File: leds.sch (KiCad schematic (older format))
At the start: 32 parts

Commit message: start working on spokes
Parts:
- added D33, D34, D35, D36, D37, D38, D39, D40, D41, D42, D43, D44, D45, D46, D47, D48, D49, D50, D51, D52, D53, D54, D55, D56, D57, D58, D59, D60, D61, D62, D63, D64, D65, D66, D67, D68, D69, D70, D71, D72, D73, D74, D75, D76, D77, D78, D79, D80, D? (x16): APA102-2020, LED_SMD:LED-APA102-2020_tightened_pads, symbol LED:APA102-2020
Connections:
- net +5V: now also D33.1 (VDD), D34.1 (VDD), D35.1 (VDD), D36.1 (VDD), D37.1 (VDD), D38.1 (VDD), D39.1 (VDD), D40.1 (VDD), D41.1 (VDD), D42.1 (VDD), D43.1 (VDD), D44.1 (VDD), D45.1 (VDD), D46.1 (VDD), D47.1 (VDD), D48.1 (VDD), D49.1 (VDD), D50.1 (VDD), D51.1 (VDD), D52.1 (VDD), D53.1 (VDD), D54.1 (VDD), D55.1 (VDD), D56.1 (VDD), D57.1 (VDD), D58.1 (VDD), D59.1 (VDD), D60.1 (VDD), D61.1 (VDD), D62.1 (VDD), D63.1 (VDD), D64.1 (VDD), D65.1 (VDD), D66.1 (VDD), D67.1 (VDD), D68.1 (VDD), D69.1 (VDD), D70.1 (VDD), D71.1 (VDD), D72.1 (VDD), D73.1 (VDD), D74.1 (VDD), D75.1 (VDD), D76.1 (VDD), D77.1 (VDD), D78.1 (VDD), D79.1 (VDD), D80.1 (VDD), D?.1 (VDD), D?.1 (VDD), D?.1 (VDD), D?.1 (VDD), D?.1 (VDD), D?.1 (VDD), D?.1 (VDD), D?.1 (VDD), D?.1 (VDD), D?.1 (VDD), D?.1 (VDD), D?.1 (VDD), D?.1 (VDD), D?.1 (VDD), D?.1 (VDD), D?.1 (VDD)
- net GND: now also D33.6 (GND), D34.6 (GND), D35.6 (GND), D36.6 (GND), D37.6 (GND), D38.6 (GND), D39.6 (GND), D40.6 (GND), D41.6 (GND), D42.6 (GND), D43.6 (GND), D44.6 (GND), D45.6 (GND), D46.6 (GND), D47.6 (GND), D48.6 (GND), D49.6 (GND), D50.6 (GND), D51.6 (GND), D52.6 (GND), D53.6 (GND), D54.6 (GND), D55.6 (GND), D56.6 (GND), D57.6 (GND), D58.6 (GND), D59.6 (GND), D60.6 (GND), D61.6 (GND), D62.6 (GND), D63.6 (GND), D64.6 (GND), D65.6 (GND), D66.6 (GND), D67.6 (GND), D68.6 (GND), D69.6 (GND), D70.6 (GND), D71.6 (GND), D72.6 (GND), D73.6 (GND), D74.6 (GND), D75.6 (GND), D76.6 (GND), D77.6 (GND), D78.6 (GND), D79.6 (GND), D80.6 (GND), D?.6 (GND), D?.6 (GND), D?.6 (GND), D?.6 (GND), D?.6 (GND), D?.6 (GND), D?.6 (GND), D?.6 (GND), D?.6 (GND), D?.6 (GND), D?.6 (GND), D?.6 (GND), D?.6 (GND), D?.6 (GND), D?.6 (GND), D?.6 (GND)
- net D32_CKO: now reaches D32.2 (CKO)
- net D32_CKO: now also D33.5 (CKI)
- net D32_SDO: now reaches D32.3 (SDO)
- net D32_SDO: now also D33.4 (SDI)
- net SCK renamed LED_SCK
- net SDO renamed LED_DATA
- new net: D48.2 (CKO), D49.5 (CKI)
- new net: D48.3 (SDO), D49.4 (SDI)
- new net: D47.3 (SDO), D48.4 (SDI)
- new net: D47.2 (CKO), D48.5 (CKI)
- new net: D46.3 (SDO), D47.4 (SDI)
- new net: D46.2 (CKO), D47.5 (CKI)
- new net: D45.3 (SDO), D46.4 (SDI)
- new net: D45.2 (CKO), D46.5 (CKI)
- new net: D44.3 (SDO), D45.4 (SDI)
- new net: D44.2 (CKO), D45.5 (CKI)
- new net: D43.3 (SDO), D44.4 (SDI)
- new net: D43.2 (CKO), D44.5 (CKI)
- new net: D42.3 (SDO), D43.4 (SDI)
- new net: D42.2 (CKO), D43.5 (CKI)
- new net: D41.3 (SDO), D42.4 (SDI)
- new net: D41.2 (CKO), D42.5 (CKI)
- new net: D40.3 (SDO), D41.4 (SDI)
- new net: D40.2 (CKO), D41.5 (CKI)
- new net: D39.3 (SDO), D40.4 (SDI)
- new net: D39.2 (CKO), D40.5 (CKI)
- new net: D38.3 (SDO), D39.4 (SDI)
- new net: D38.2 (CKO), D39.5 (CKI)
- new net: D37.3 (SDO), D38.4 (SDI)
- new net: D37.2 (CKO), D38.5 (CKI)
- new net: D36.3 (SDO), D37.4 (SDI)
- new net: D36.2 (CKO), D37.5 (CKI)
- new net: D35.3 (SDO), D36.4 (SDI)
- new net: D35.2 (CKO), D36.5 (CKI)
- new net: D34.3 (SDO), D35.4 (SDI)
- new net: D34.2 (CKO), D35.5 (CKI)
- new net: D33.3 (SDO), D34.4 (SDI)
- new net: D33.2 (CKO), D34.5 (CKI)
- new net: D49.2 (CKO), D50.5 (CKI)
- new net: D49.3 (SDO), D50.4 (SDI)
- new net: D50.2 (CKO), D51.5 (CKI)
- new net: D50.3 (SDO), D51.4 (SDI)
- new net: D51.2 (CKO), D52.5 (CKI)
- new net: D51.3 (SDO), D52.4 (SDI)
- new net: D52.2 (CKO), D53.5 (CKI)
- new net: D52.3 (SDO), D53.4 (SDI)
- new net: D53.2 (CKO), D54.5 (CKI)
- new net: D53.3 (SDO), D54.4 (SDI)
- new net: D54.2 (CKO), D55.5 (CKI)
- new net: D54.3 (SDO), D55.4 (SDI)
- new net: D55.2 (CKO), D56.5 (CKI)
- new net: D55.3 (SDO), D56.4 (SDI)
- new net: D56.2 (CKO), D57.5 (CKI)
- new net: D56.3 (SDO), D57.4 (SDI)
- new net: D57.2 (CKO), D58.5 (CKI)
- new net: D57.3 (SDO), D58.4 (SDI)
- new net: D58.2 (CKO), D59.5 (CKI)
- new net: D58.3 (SDO), D59.4 (SDI)
- new net: D59.2 (CKO), D60.5 (CKI)
- new net: D59.3 (SDO), D60.4 (SDI)
- new net: D60.2 (CKO), D61.5 (CKI)
- new net: D60.3 (SDO), D61.4 (SDI)
- new net: D61.2 (CKO), D62.5 (CKI)
- new net: D61.3 (SDO), D62.4 (SDI)
- new net: D62.2 (CKO), D63.5 (CKI)
- new net: D62.3 (SDO), D63.4 (SDI)
- new net: D63.2 (CKO), D64.5 (CKI)
- new net: D63.3 (SDO), D64.4 (SDI)
- new net: D80.2 (CKO), D?.5 (CKI)
- new net: D80.3 (SDO), D?.4 (SDI)
- new net: D79.3 (SDO), D80.4 (SDI)
- new net: D79.2 (CKO), D80.5 (CKI)
- new net: D78.3 (SDO), D79.4 (SDI)
- new net: D78.2 (CKO), D79.5 (CKI)
- new net: D77.3 (SDO), D78.4 (SDI)
- new net: D77.2 (CKO), D78.5 (CKI)
- new net: D76.3 (SDO), D77.4 (SDI)
- new net: D76.2 (CKO), D77.5 (CKI)
- new net: D75.3 (SDO), D76.4 (SDI)
- new net: D75.2 (CKO), D76.5 (CKI)
- new net: D74.3 (SDO), D75.4 (SDI)
- new net: D74.2 (CKO), D75.5 (CKI)
- new net: D73.3 (SDO), D74.4 (SDI)
- new net: D73.2 (CKO), D74.5 (CKI)
- new net: D72.3 (SDO), D73.4 (SDI)
- new net: D72.2 (CKO), D73.5 (CKI)
- new net: D71.3 (SDO), D72.4 (SDI)
- new net: D71.2 (CKO), D72.5 (CKI)
- new net: D70.3 (SDO), D71.4 (SDI)
- new net: D70.2 (CKO), D71.5 (CKI)
- new net: D69.3 (SDO), D70.4 (SDI)
- new net: D69.2 (CKO), D70.5 (CKI)
- new net: D68.3 (SDO), D69.4 (SDI)
- new net: D68.2 (CKO), D69.5 (CKI)
- new net: D67.3 (SDO), D68.4 (SDI)
- new net: D67.2 (CKO), D68.5 (CKI)
- new net: D66.3 (SDO), D67.4 (SDI)
- new net: D66.2 (CKO), D67.5 (CKI)
- new net: D65.3 (SDO), D66.4 (SDI)
- new net: D65.2 (CKO), D66.5 (CKI)
- new net: D?.2 (CKO), D?.5 (CKI) (x15)
- new net: D?.3 (SDO), D?.4 (SDI) (x15)
- new net D64_CKO: D64.2 (CKO), D65.5 (CKI)
- new net D64_SDO: D64.3 (SDO), D65.4 (SDI)

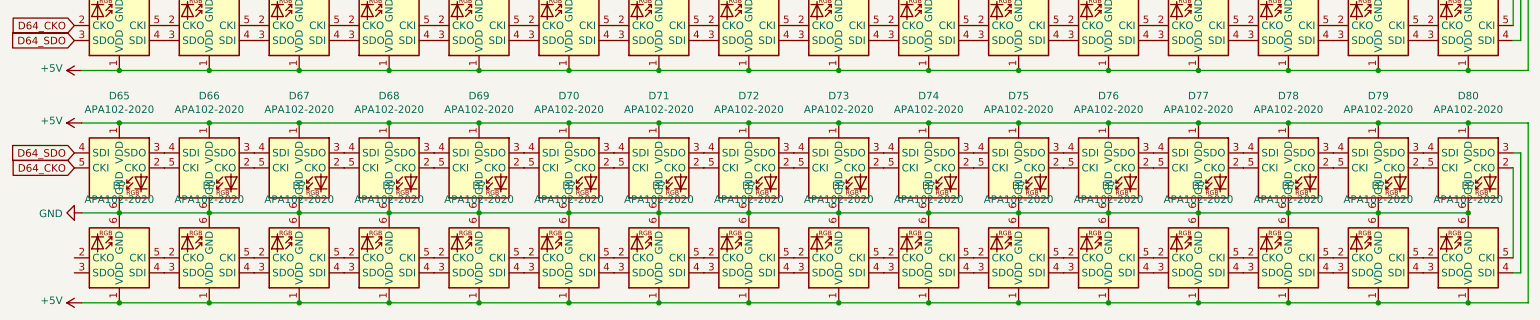
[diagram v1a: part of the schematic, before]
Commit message: clean up various point-like object types; tweak Edge.Cuts to be precise overlap in order to fix pcbnew thinking it wasn't a closed shape, but turns out this was also a bug fixed in kicad-5.1.3 so I'm not sure if this change was actually necessary, but it works now
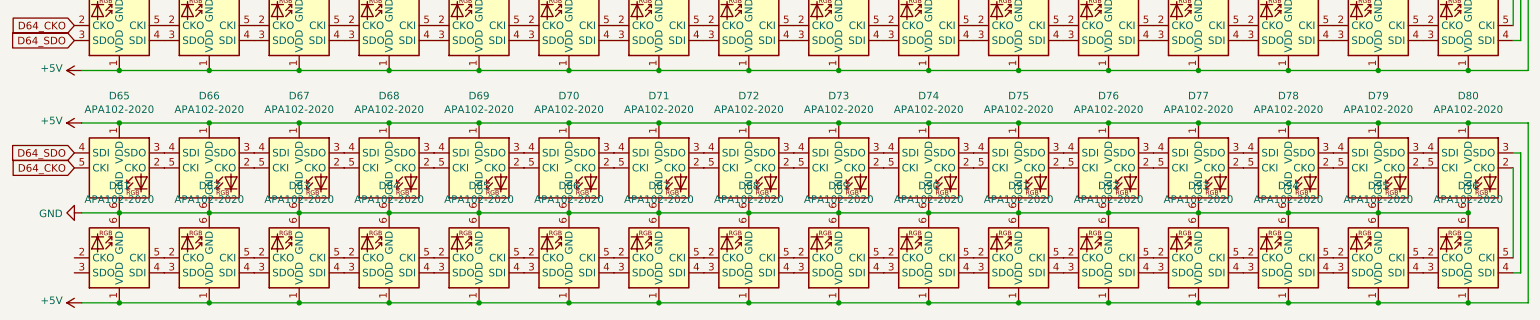
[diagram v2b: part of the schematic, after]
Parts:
- gave numbers to parts that had none: 16
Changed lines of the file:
@@
 P 10100 4900
 AR Path="/5F992E17" Ref="D?"  Part="1"
-AR Path="/5F81AC32/5F992E17" Ref="D?"  Part="1"
-F 0 "D?" H 10100 4419 50  0000 C CNN
+AR Path="/5F81AC32/5F992E17" Ref="D96"  Part="1"
+F 0 "D96" H 10100 4419 50  0000 C CNN
 F 1 "APA102-2020" H 10100 4510 50  0000 C CNN
 F 2 "LED_SMD:LED-APA102-2020_tightened_pads" H 10150 4600 50  0001 L TNN
@@
 P 9500 4900
 AR Path="/5F992E1D" Ref="D?"  Part="1"
-AR Path="/5F81AC32/5F992E1D" Ref="D?"  Part="1"
-F 0 "D?" H 9500 4419 50  0000 C CNN
+AR Path="/5F81AC32/5F992E1D" Ref="D95"  Part="1"
+F 0 "D95" H 9500 4419 50  0000 C CNN
 F 1 "APA102-2020" H 9500 4510 50  0000 C CNN
 F 2 "LED_SMD:LED-APA102-2020_tightened_pads" H 9550 4600 50  0001 L TNN
@@
 P 8900 4900
 AR Path="/5F992E26" Ref="D?"  Part="1"
-AR Path="/5F81AC32/5F992E26" Ref="D?"  Part="1"
-F 0 "D?" H 8900 4419 50  0000 C CNN
+AR Path="/5F81AC32/5F992E26" Ref="D94"  Part="1"
+F 0 "D94" H 8900 4419 50  0000 C CNN
 F 1 "APA102-2020" H 8900 4510 50  0000 C CNN
 F 2 "LED_SMD:LED-APA102-2020_tightened_pads" H 8950 4600 50  0001 L TNN
@@
 P 8300 4900
 AR Path="/5F992E2C" Ref="D?"  Part="1"
-AR Path="/5F81AC32/5F992E2C" Ref="D?"  Part="1"
-F 0 "D?" H 8300 4419 50  0000 C CNN
+AR Path="/5F81AC32/5F992E2C" Ref="D93"  Part="1"
+F 0 "D93" H 8300 4419 50  0000 C CNN
 F 1 "APA102-2020" H 8300 4510 50  0000 C CNN
 F 2 "LED_SMD:LED-APA102-2020_tightened_pads" H 8350 4600 50  0001 L TNN
@@
 P 7700 4900
 AR Path="/5F992E32" Ref="D?"  Part="1"
-AR Path="/5F81AC32/5F992E32" Ref="D?"  Part="1"
-F 0 "D?" H 7700 4419 50  0000 C CNN
+AR Path="/5F81AC32/5F992E32" Ref="D92"  Part="1"
+F 0 "D92" H 7700 4419 50  0000 C CNN
 F 1 "APA102-2020" H 7700 4510 50  0000 C CNN
 F 2 "LED_SMD:LED-APA102-2020_tightened_pads" H 7750 4600 50  0001 L TNN
@@
 P 7100 4900
 AR Path="/5F992E38" Ref="D?"  Part="1"
-AR Path="/5F81AC32/5F992E38" Ref="D?"  Part="1"
-F 0 "D?" H 7100 4419 50  0000 C CNN
+AR Path="/5F81AC32/5F992E38" Ref="D91"  Part="1"
+F 0 "D91" H 7100 4419 50  0000 C CNN
 F 1 "APA102-2020" H 7100 4510 50  0000 C CNN
 F 2 "LED_SMD:LED-APA102-2020_tightened_pads" H 7150 4600 50  0001 L TNN
@@
 P 6500 4900
 AR Path="/5F992E3E" Ref="D?"  Part="1"
-AR Path="/5F81AC32/5F992E3E" Ref="D?"  Part="1"
-F 0 "D?" H 6500 4419 50  0000 C CNN
+AR Path="/5F81AC32/5F992E3E" Ref="D90"  Part="1"
+F 0 "D90" H 6500 4419 50  0000 C CNN
 F 1 "APA102-2020" H 6500 4510 50  0000 C CNN
 F 2 "LED_SMD:LED-APA102-2020_tightened_pads" H 6550 4600 50  0001 L TNN
@@
 P 5900 4900
 AR Path="/5F992E44" Ref="D?"  Part="1"
-AR Path="/5F81AC32/5F992E44" Ref="D?"  Part="1"
-F 0 "D?" H 5900 4419 50  0000 C CNN
+AR Path="/5F81AC32/5F992E44" Ref="D89"  Part="1"
+F 0 "D89" H 5900 4419 50  0000 C CNN
 F 1 "APA102-2020" H 5900 4510 50  0000 C CNN
 F 2 "LED_SMD:LED-APA102-2020_tightened_pads" H 5950 4600 50  0001 L TNN
@@
 P 5300 4900
 AR Path="/5F992E4A" Ref="D?"  Part="1"
-AR Path="/5F81AC32/5F992E4A" Ref="D?"  Part="1"
-F 0 "D?" H 5300 4419 50  0000 C CNN
+AR Path="/5F81AC32/5F992E4A" Ref="D88"  Part="1"
+F 0 "D88" H 5300 4419 50  0000 C CNN
 F 1 "APA102-2020" H 5300 4510 50  0000 C CNN
 F 2 "LED_SMD:LED-APA102-2020_tightened_pads" H 5350 4600 50  0001 L TNN
@@
 P 4700 4900
 AR Path="/5F992E50" Ref="D?"  Part="1"
-AR Path="/5F81AC32/5F992E50" Ref="D?"  Part="1"
-F 0 "D?" H 4700 4419 50  0000 C CNN
+AR Path="/5F81AC32/5F992E50" Ref="D87"  Part="1"
+F 0 "D87" H 4700 4419 50  0000 C CNN
 F 1 "APA102-2020" H 4700 4510 50  0000 C CNN
 F 2 "LED_SMD:LED-APA102-2020_tightened_pads" H 4750 4600 50  0001 L TNN
@@
 P 4100 4900
 AR Path="/5F992E56" Ref="D?"  Part="1"
-AR Path="/5F81AC32/5F992E56" Ref="D?"  Part="1"
-F 0 "D?" H 4100 4419 50  0000 C CNN
+AR Path="/5F81AC32/5F992E56" Ref="D86"  Part="1"
+F 0 "D86" H 4100 4419 50  0000 C CNN
 F 1 "APA102-2020" H 4100 4510 50  0000 C CNN
 F 2 "LED_SMD:LED-APA102-2020_tightened_pads" H 4150 4600 50  0001 L TNN
@@
 P 3500 4900
 AR Path="/5F992E5C" Ref="D?"  Part="1"
-AR Path="/5F81AC32/5F992E5C" Ref="D?"  Part="1"
-F 0 "D?" H 3500 4419 50  0000 C CNN
+AR Path="/5F81AC32/5F992E5C" Ref="D85"  Part="1"
+F 0 "D85" H 3500 4419 50  0000 C CNN
 F 1 "APA102-2020" H 3500 4510 50  0000 C CNN
 F 2 "LED_SMD:LED-APA102-2020_tightened_pads" H 3550 4600 50  0001 L TNN
@@
 P 2900 4900
 AR Path="/5F992E62" Ref="D?"  Part="1"
-AR Path="/5F81AC32/5F992E62" Ref="D?"  Part="1"
-F 0 "D?" H 2900 4419 50  0000 C CNN
+AR Path="/5F81AC32/5F992E62" Ref="D84"  Part="1"
+F 0 "D84" H 2900 4419 50  0000 C CNN
 F 1 "APA102-2020" H 2900 4510 50  0000 C CNN
 F 2 "LED_SMD:LED-APA102-2020_tightened_pads" H 2950 4600 50  0001 L TNN
@@
 P 2300 4900
 AR Path="/5F992E68" Ref="D?"  Part="1"
-AR Path="/5F81AC32/5F992E68" Ref="D?"  Part="1"
-F 0 "D?" H 2300 4419 50  0000 C CNN
+AR Path="/5F81AC32/5F992E68" Ref="D83"  Part="1"
+F 0 "D83" H 2300 4419 50  0000 C CNN
 F 1 "APA102-2020" H 2300 4510 50  0000 C CNN
 F 2 "LED_SMD:LED-APA102-2020_tightened_pads" H 2350 4600 50  0001 L TNN
@@
 P 1700 4900
 AR Path="/5F992E6E" Ref="D?"  Part="1"
-AR Path="/5F81AC32/5F992E6E" Ref="D?"  Part="1"
-F 0 "D?" H 1700 4419 50  0000 C CNN
+AR Path="/5F81AC32/5F992E6E" Ref="D82"  Part="1"
+F 0 "D82" H 1700 4419 50  0000 C CNN
 F 1 "APA102-2020" H 1700 4510 50  0000 C CNN
 F 2 "LED_SMD:LED-APA102-2020_tightened_pads" H 1750 4600 50  0001 L TNN
@@
 P 1100 4900
 AR Path="/5F992E74" Ref="D?"  Part="1"
-AR Path="/5F81AC32/5F992E74" Ref="D?"  Part="1"
-F 0 "D?" H 1100 4419 50  0000 C CNN
+AR Path="/5F81AC32/5F992E74" Ref="D81"  Part="1"
+F 0 "D81" H 1100 4419 50  0000 C CNN
 F 1 "APA102-2020" H 1100 4510 50  0000 C CNN
 F 2 "LED_SMD:LED-APA102-2020_tightened_pads" H 1150 4600 50  0001 L TNN
@@
 $EndComp
 $Comp
-L power:+5V #PWR?
+L power:+5V #PWR0124
 U 1 1 5F992E7A
 P 850 5200
-F 0 "#PWR?" H 850 5050 50  0001 C CNN
+F 0 "#PWR0124" H 850 5050 50  0001 C CNN
 F 1 "+5V" V 865 5328 50  0000 L CNN
 F 2 "" H 850 5200 50  0001 C CNN
@@
 	1100 4600 850  4600
 $Comp
-L power:GND #PWR?
+L power:GND #PWR0125
 U 1 1 5F9ECE1D
 P 850 3050
-F 0 "#PWR?" H 850 2800 50  0001 C CNN
+F 0 "#PWR0125" H 850 2800 50  0001 C CNN
 F 1 "GND" V 855 2922 50  0000 R CNN
 F 2 "" H 850 3050 50  0001 C CNN

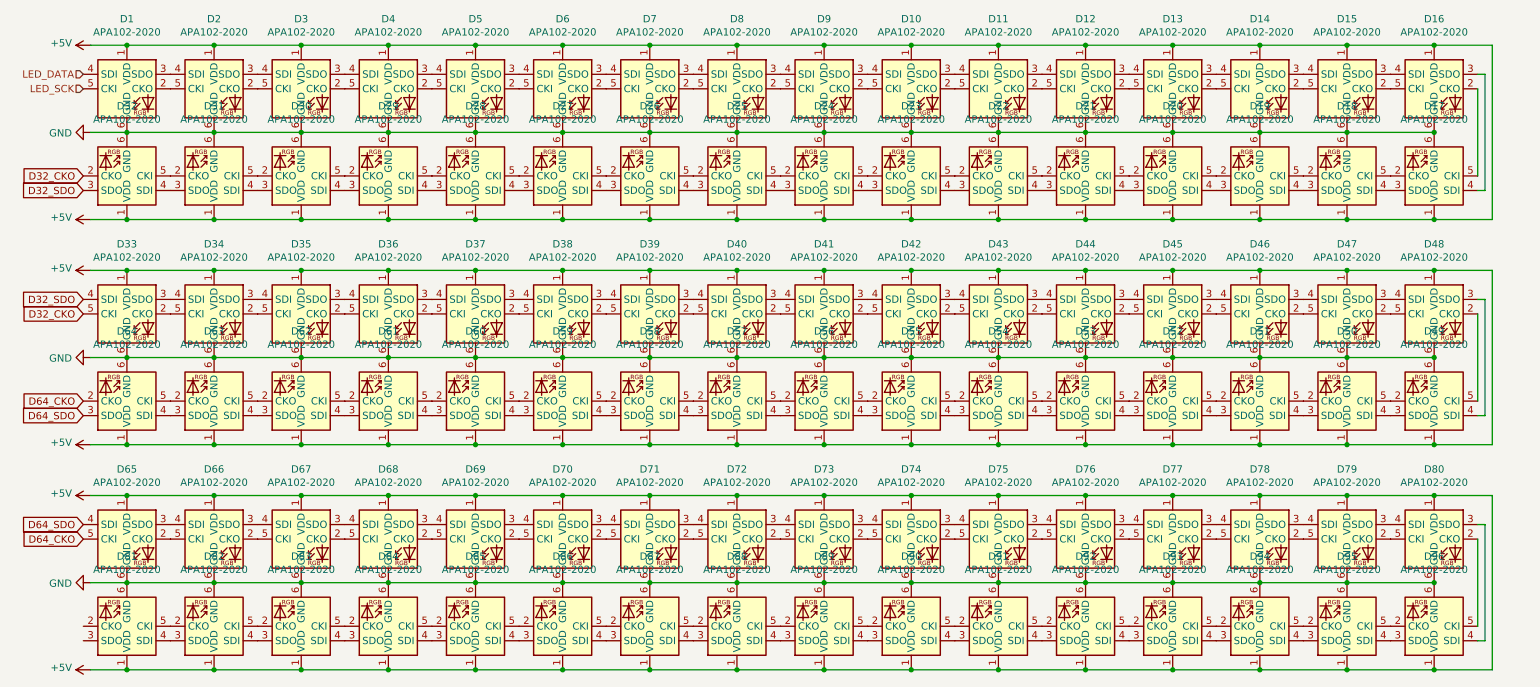
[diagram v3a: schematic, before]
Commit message: first pass on manual layout of board including led power traces & samd circuitry; key idea: take out the usb port and solder the usb data & power directly to the board, i.e. it'll have its own cable attached, possibly a short cable with the usb plug on it so that I can use various length usb cables
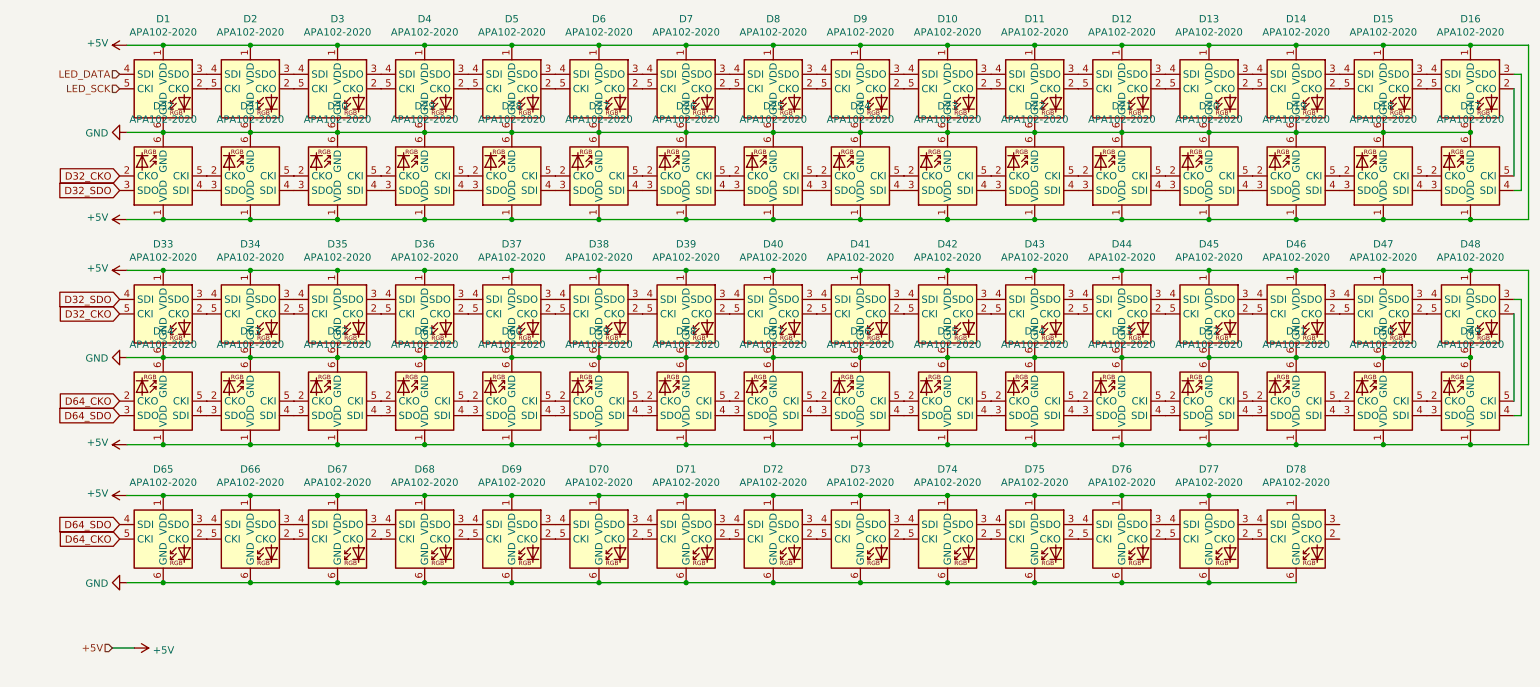
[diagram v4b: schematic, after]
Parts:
- removed D79, D80, D81, D82, D83, D84, D85, D86, D87, D88, D89, D90, D91, D92, D93, D94, D95, D96: APA102-2020, LED_SMD:LED-APA102-2020_tightened_pads, symbol LED:APA102-2020
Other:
- moved on the sheet: D1, D10, D11, D12, D13, D14, D15, D16, D17, D18, D19, D2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

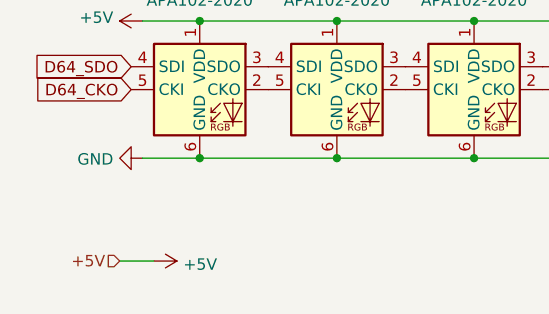
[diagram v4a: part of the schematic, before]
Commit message: add a decoupling capacitor on +5V for LEDs
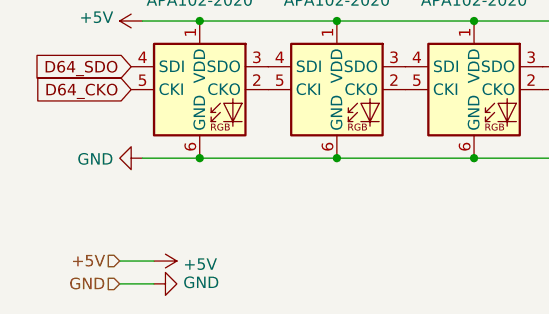
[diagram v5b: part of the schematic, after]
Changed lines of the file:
@@
 +5V
 $Comp
-L power:+5V #PWR?
+L power:+5V #PWR0126
 U 1 1 5FA6C532
 P 1150 5050
-F 0 "#PWR?" H 1150 4900 50  0001 C CNN
+F 0 "#PWR0126" H 1150 4900 50  0001 C CNN
 F 1 "+5V" V 1165 5178 50  0000 L CNN
 F 2 "" H 1150 5050 50  0001 C CNN
@@
 Wire Wire Line
 	1000 5050 1150 5050
+Text HLabel 1000 5150 0    50   Input ~ 0
+GND
+$Comp
+L power:GND #PWR0128
+U 1 1 5FBD3D30
+P 1150 5150
+F 0 "#PWR0128" H 1150 4900 50  0001 C CNN
+F 1 "GND" V 1155 5022 50  0000 R CNN
+F 2 "" H 1150 5150 50  0001 C CNN
+F 3 "" H 1150 5150 50  0001 C CNN
+	1    1150 5150
+	0    -1   -1   0
+$EndComp
+Wire Wire Line
+	1000 5150 1150 5150
 $EndSCHEMATC
